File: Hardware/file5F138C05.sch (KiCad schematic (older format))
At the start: 7 parts

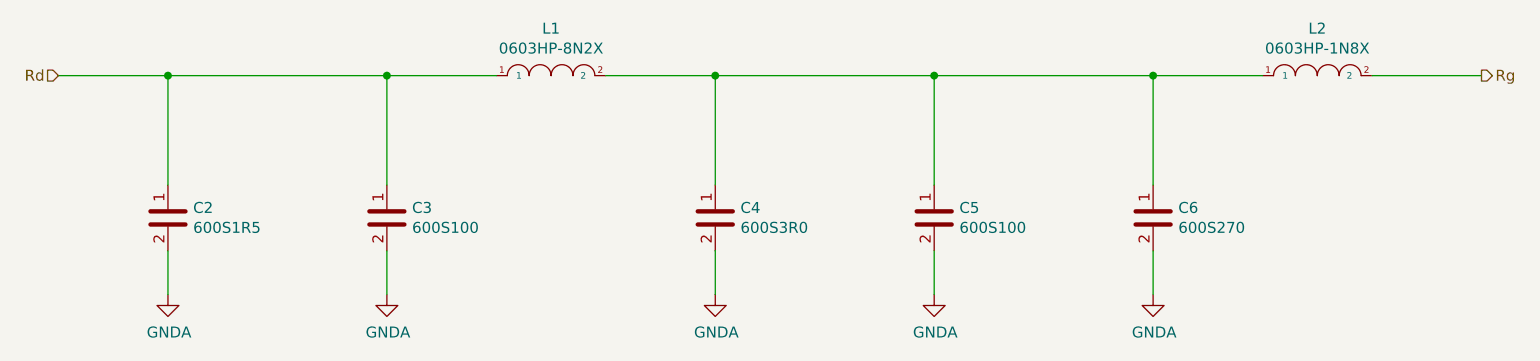
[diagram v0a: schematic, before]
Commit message: Added discrete Chebyshev input filter to schematic based on Qucs simulationd. Artwork not done. It has occurred to me that I need to do some major cleanup of the test points on this PCBA.
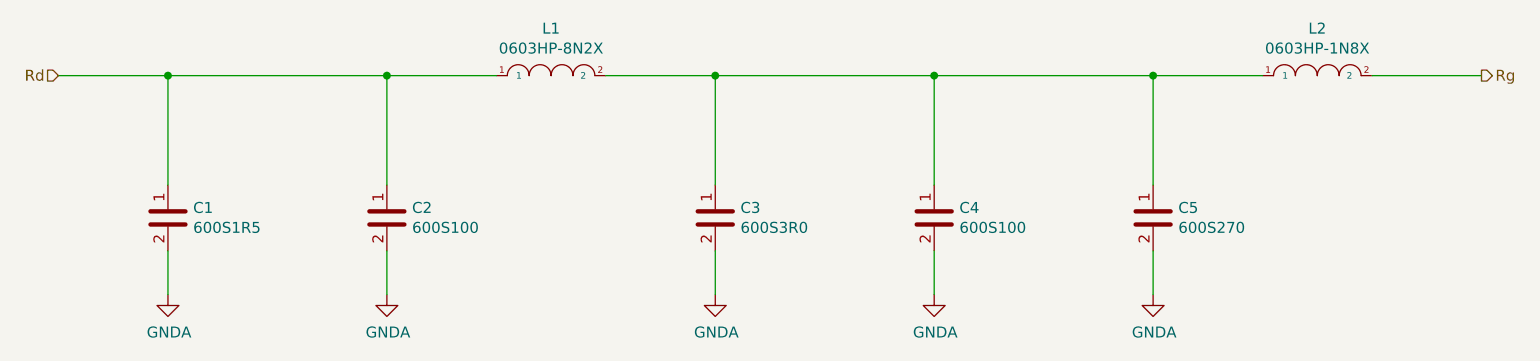
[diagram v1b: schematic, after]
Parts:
- renumbered C2 to C1, C3 to C2, C4 to C3, C5 to C4, C6 to C5
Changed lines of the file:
@@
 $Descr A4 11693 8268
 encoding utf-8
-Sheet 5 12
+Sheet 5 16
 Title ""
 Date ""
@@
 Rg
 $Comp
-L ATC:600S1R5 C2
+L ATC:600S1R5 C1
 U 1 1 5F152659
 P 3000 4150
-F 0 "C2" H 3115 4196 50  0000 L CNN
+F 0 "C1" H 3115 4196 50  0000 L CNN
 F 1 "600S1R5" H 3115 4105 50  0000 L CNN
 F 2 "Capacitor_SMD:C_0603_1608Metric" H 3050 4250 50  0001 C CNN
@@
 $EndComp
 $Comp
-L ATC:600S100 C3
+L ATC:600S100 C2
 U 1 1 5F152A8E
 P 4000 4150
-F 0 "C3" H 4115 4196 50  0000 L CNN
+F 0 "C2" H 4115 4196 50  0000 L CNN
 F 1 "600S100" H 4115 4105 50  0000 L CNN
 F 2 "Capacitor_SMD:C_0603_1608Metric" H 4050 4250 50  0001 C CNN
@@
 $EndComp
 $Comp
-L ATC:600S3R0 C4
+L ATC:600S3R0 C3
 U 1 1 5F152CBF
 P 5500 4150
-F 0 "C4" H 5615 4196 50  0000 L CNN
+F 0 "C3" H 5615 4196 50  0000 L CNN
 F 1 "600S3R0" H 5615 4105 50  0000 L CNN
 F 2 "Capacitor_SMD:C_0603_1608Metric" H 5550 4250 50  0001 C CNN
@@
 $EndComp
 $Comp
-L ATC:600S100 C5
+L ATC:600S100 C4
 U 1 1 5F152F10
 P 6500 4150
-F 0 "C5" H 6615 4196 50  0000 L CNN
+F 0 "C4" H 6615 4196 50  0000 L CNN
 F 1 "600S100" H 6615 4105 50  0000 L CNN
 F 2 "Capacitor_SMD:C_0603_1608Metric" H 6550 4250 50  0001 C CNN
@@
 $EndComp
 $Comp
-L ATC:600S270 C6
+L ATC:600S270 C5
 U 1 1 5F15313B
 P 7500 4150
-F 0 "C6" H 7615 4196 50  0000 L CNN
+F 0 "C5" H 7615 4196 50  0000 L CNN
 F 1 "600S270" H 7615 4105 50  0000 L CNN
 F 2 "Capacitor_SMD:C_0603_1608Metric" H 7550 4250 50  0001 C CNN
@@
 AR Path="/5F19ABE9/5F15450B" Ref="#PWR?"  Part="1"
 AR Path="/5F04F5B6/5F15450B" Ref="#PWR?"  Part="1"
-AR Path="/5F04F5B6/5F138C06/5F15450B" Ref="#PWR09"  Part="1"
-F 0 "#PWR09" H 3000 4250 50  0001 C CNN
+AR Path="/5F04F5B6/5F138C06/5F15450B" Ref="#PWR06"  Part="1"
+F 0 "#PWR06" H 3000 4250 50  0001 C CNN
 F 1 "GNDA" H 3005 4327 50  0000 C CNN
 F 2 "" H 3000 4500 50  0001 C CNN
@@
 AR Path="/5F19ABE9/5F154511" Ref="#PWR?"  Part="1"
 AR Path="/5F04F5B6/5F154511" Ref="#PWR?"  Part="1"
-AR Path="/5F04F5B6/5F138C06/5F154511" Ref="#PWR010"  Part="1"
-F 0 "#PWR010" H 4000 4250 50  0001 C CNN
+AR Path="/5F04F5B6/5F138C06/5F154511" Ref="#PWR07"  Part="1"
+F 0 "#PWR07" H 4000 4250 50  0001 C CNN
 F 1 "GNDA" H 4005 4327 50  0000 C CNN
 F 2 "" H 4000 4500 50  0001 C CNN
@@
 AR Path="/5F19ABE9/5F1549C9" Ref="#PWR?"  Part="1"
 AR Path="/5F04F5B6/5F1549C9" Ref="#PWR?"  Part="1"
-AR Path="/5F04F5B6/5F138C06/5F1549C9" Ref="#PWR011"  Part="1"
-F 0 "#PWR011" H 5500 4250 50  0001 C CNN
+AR Path="/5F04F5B6/5F138C06/5F1549C9" Ref="#PWR08"  Part="1"
+F 0 "#PWR08" H 5500 4250 50  0001 C CNN
 F 1 "GNDA" H 5505 4327 50  0000 C CNN
 F 2 "" H 5500 4500 50  0001 C CNN
@@
 AR Path="/5F19ABE9/5F1549CF" Ref="#PWR?"  Part="1"
 AR Path="/5F04F5B6/5F1549CF" Ref="#PWR?"  Part="1"
-AR Path="/5F04F5B6/5F138C06/5F1549CF" Ref="#PWR012"  Part="1"
-F 0 "#PWR012" H 6500 4250 50  0001 C CNN
+AR Path="/5F04F5B6/5F138C06/5F1549CF" Ref="#PWR09"  Part="1"
+F 0 "#PWR09" H 6500 4250 50  0001 C CNN
 F 1 "GNDA" H 6505 4327 50  0000 C CNN
 F 2 "" H 6500 4500 50  0001 C CNN
@@
 AR Path="/5F19ABE9/5F154DAF" Ref="#PWR?"  Part="1"
 AR Path="/5F04F5B6/5F154DAF" Ref="#PWR?"  Part="1"
-AR Path="/5F04F5B6/5F138C06/5F154DAF" Ref="#PWR013"  Part="1"
-F 0 "#PWR013" H 7500 4250 50  0001 C CNN
+AR Path="/5F04F5B6/5F138C06/5F154DAF" Ref="#PWR010"  Part="1"
+F 0 "#PWR010" H 7500 4250 50  0001 C CNN
 F 1 "GNDA" H 7505 4327 50  0000 C CNN
 F 2 "" H 7500 4500 50  0001 C CNN

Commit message: Major cleanup to both the schematic and directory structure. Stackup has changed accomodate to 0.65mm trace width. Chebyshev filter lived through the experience in the Qucs simulation; others not checked yet. I do want to re-visit the matching networks of all of the amplifiers as I have developed some good strategies to implement them.
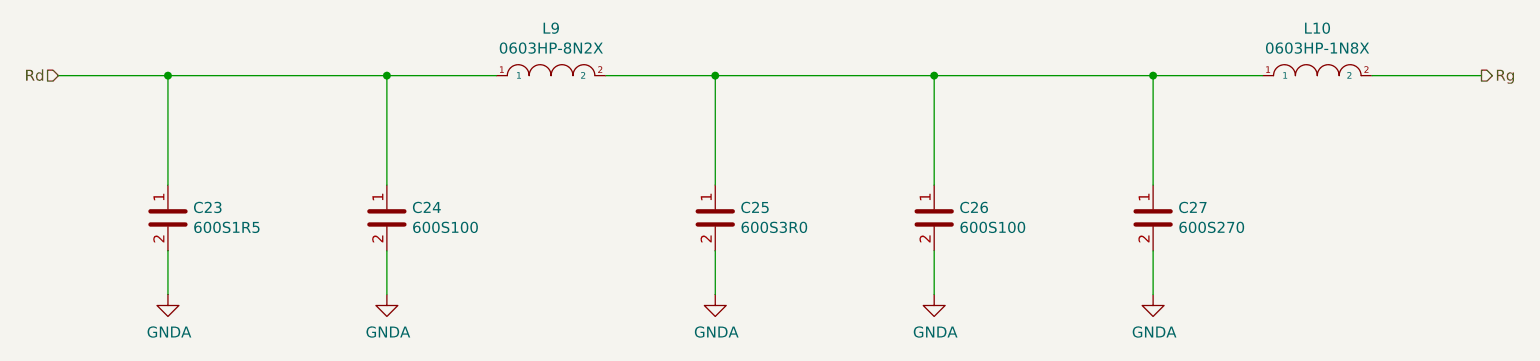
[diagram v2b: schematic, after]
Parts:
- renumbered C1 to C23, C2 to C24, C3 to C25, C4 to C26, C5 to C27, L2 to L10, L1 to L9
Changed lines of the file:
@@
 $Descr A4 11693 8268
 encoding utf-8
-Sheet 5 16
+Sheet 16 24
 Title ""
 Date ""
@@
 Rg
 $Comp
-L ATC:600S1R5 C1
+L ATC:600S1R5 C23
 U 1 1 5F152659
 P 3000 4150
-F 0 "C1" H 3115 4196 50  0000 L CNN
+F 0 "C23" H 3115 4196 50  0000 L CNN
 F 1 "600S1R5" H 3115 4105 50  0000 L CNN
 F 2 "Capacitor_SMD:C_0603_1608Metric" H 3050 4250 50  0001 C CNN
@@
 $EndComp
 $Comp
-L ATC:600S100 C2
+L ATC:600S100 C24
 U 1 1 5F152A8E
 P 4000 4150
-F 0 "C2" H 4115 4196 50  0000 L CNN
+F 0 "C24" H 4115 4196 50  0000 L CNN
 F 1 "600S100" H 4115 4105 50  0000 L CNN
 F 2 "Capacitor_SMD:C_0603_1608Metric" H 4050 4250 50  0001 C CNN
@@
 $EndComp
 $Comp
-L ATC:600S3R0 C3
+L ATC:600S3R0 C25
 U 1 1 5F152CBF
 P 5500 4150
-F 0 "C3" H 5615 4196 50  0000 L CNN
+F 0 "C25" H 5615 4196 50  0000 L CNN
 F 1 "600S3R0" H 5615 4105 50  0000 L CNN
 F 2 "Capacitor_SMD:C_0603_1608Metric" H 5550 4250 50  0001 C CNN
@@
 $EndComp
 $Comp
-L ATC:600S100 C4
+L ATC:600S100 C26
 U 1 1 5F152F10
 P 6500 4150
-F 0 "C4" H 6615 4196 50  0000 L CNN
+F 0 "C26" H 6615 4196 50  0000 L CNN
 F 1 "600S100" H 6615 4105 50  0000 L CNN
 F 2 "Capacitor_SMD:C_0603_1608Metric" H 6550 4250 50  0001 C CNN
@@
 $EndComp
 $Comp
-L ATC:600S270 C5
+L ATC:600S270 C27
 U 1 1 5F15313B
 P 7500 4150
-F 0 "C5" H 7615 4196 50  0000 L CNN
+F 0 "C27" H 7615 4196 50  0000 L CNN
 F 1 "600S270" H 7615 4105 50  0000 L CNN
 F 2 "Capacitor_SMD:C_0603_1608Metric" H 7550 4250 50  0001 C CNN
@@
 $EndComp
 $Comp
-L Coilcraft:0603HP-8N2X L1
+L Coilcraft:0603HP-8N2X L9
 U 1 1 5F1533B1
 P 4750 3500
-F 0 "L1" H 4750 3715 50  0000 C CNN
+F 0 "L9" H 4750 3715 50  0000 C CNN
 F 1 "0603HP-8N2X" H 4750 3624 50  0000 C CNN
 F 2 "Inductor_SMD:L_0603_1608Metric" H 4500 3650 50  0001 C CNN
@@
 $EndComp
 $Comp
-L Coilcraft:0603HP-1N8X L2
+L Coilcraft:0603HP-1N8X L10
 U 1 1 5F1537BD
 P 8250 3500
-F 0 "L2" H 8250 3715 50  0000 C CNN
+F 0 "L10" H 8250 3715 50  0000 C CNN
 F 1 "0603HP-1N8X" H 8250 3624 50  0000 C CNN
 F 2 "Inductor_SMD:L_0603_1608Metric" H 8000 3650 50  0001 C CNN
@@
 AR Path="/5F19ABE9/5F15450B" Ref="#PWR?"  Part="1"
 AR Path="/5F04F5B6/5F15450B" Ref="#PWR?"  Part="1"
-AR Path="/5F04F5B6/5F138C06/5F15450B" Ref="#PWR06"  Part="1"
-F 0 "#PWR06" H 3000 4250 50  0001 C CNN
+AR Path="/5F04F5B6/5F138C06/5F15450B" Ref="#PWR?"  Part="1"
+AR Path="/5F204DEC/5F205D8E/5F138C06/5F15450B" Ref="#PWR029"  Part="1"
+F 0 "#PWR029" H 3000 4250 50  0001 C CNN
 F 1 "GNDA" H 3005 4327 50  0000 C CNN
 F 2 "" H 3000 4500 50  0001 C CNN
@@
 AR Path="/5F19ABE9/5F154511" Ref="#PWR?"  Part="1"
 AR Path="/5F04F5B6/5F154511" Ref="#PWR?"  Part="1"
-AR Path="/5F04F5B6/5F138C06/5F154511" Ref="#PWR07"  Part="1"
-F 0 "#PWR07" H 4000 4250 50  0001 C CNN
+AR Path="/5F04F5B6/5F138C06/5F154511" Ref="#PWR?"  Part="1"
+AR Path="/5F204DEC/5F205D8E/5F138C06/5F154511" Ref="#PWR030"  Part="1"
+F 0 "#PWR030" H 4000 4250 50  0001 C CNN
 F 1 "GNDA" H 4005 4327 50  0000 C CNN
 F 2 "" H 4000 4500 50  0001 C CNN
@@
 AR Path="/5F19ABE9/5F1549C9" Ref="#PWR?"  Part="1"
 AR Path="/5F04F5B6/5F1549C9" Ref="#PWR?"  Part="1"
-AR Path="/5F04F5B6/5F138C06/5F1549C9" Ref="#PWR08"  Part="1"
-F 0 "#PWR08" H 5500 4250 50  0001 C CNN
+AR Path="/5F04F5B6/5F138C06/5F1549C9" Ref="#PWR?"  Part="1"
+AR Path="/5F204DEC/5F205D8E/5F138C06/5F1549C9" Ref="#PWR031"  Part="1"
+F 0 "#PWR031" H 5500 4250 50  0001 C CNN
 F 1 "GNDA" H 5505 4327 50  0000 C CNN
 F 2 "" H 5500 4500 50  0001 C CNN
@@
 AR Path="/5F19ABE9/5F1549CF" Ref="#PWR?"  Part="1"
 AR Path="/5F04F5B6/5F1549CF" Ref="#PWR?"  Part="1"
-AR Path="/5F04F5B6/5F138C06/5F1549CF" Ref="#PWR09"  Part="1"
-F 0 "#PWR09" H 6500 4250 50  0001 C CNN
+AR Path="/5F04F5B6/5F138C06/5F1549CF" Ref="#PWR?"  Part="1"
+AR Path="/5F204DEC/5F205D8E/5F138C06/5F1549CF" Ref="#PWR032"  Part="1"
+F 0 "#PWR032" H 6500 4250 50  0001 C CNN
 F 1 "GNDA" H 6505 4327 50  0000 C CNN
 F 2 "" H 6500 4500 50  0001 C CNN
@@
 AR Path="/5F19ABE9/5F154DAF" Ref="#PWR?"  Part="1"
 AR Path="/5F04F5B6/5F154DAF" Ref="#PWR?"  Part="1"
-AR Path="/5F04F5B6/5F138C06/5F154DAF" Ref="#PWR010"  Part="1"
-F 0 "#PWR010" H 7500 4250 50  0001 C CNN
+AR Path="/5F04F5B6/5F138C06/5F154DAF" Ref="#PWR?"  Part="1"
+AR Path="/5F204DEC/5F205D8E/5F138C06/5F154DAF" Ref="#PWR033"  Part="1"
+F 0 "#PWR033" H 7500 4250 50  0001 C CNN
 F 1 "GNDA" H 7505 4327 50  0000 C CNN
 F 2 "" H 7500 4500 50  0001 C CNN

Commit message: Improving LNA simulations and Documentation package. More to come on this one.
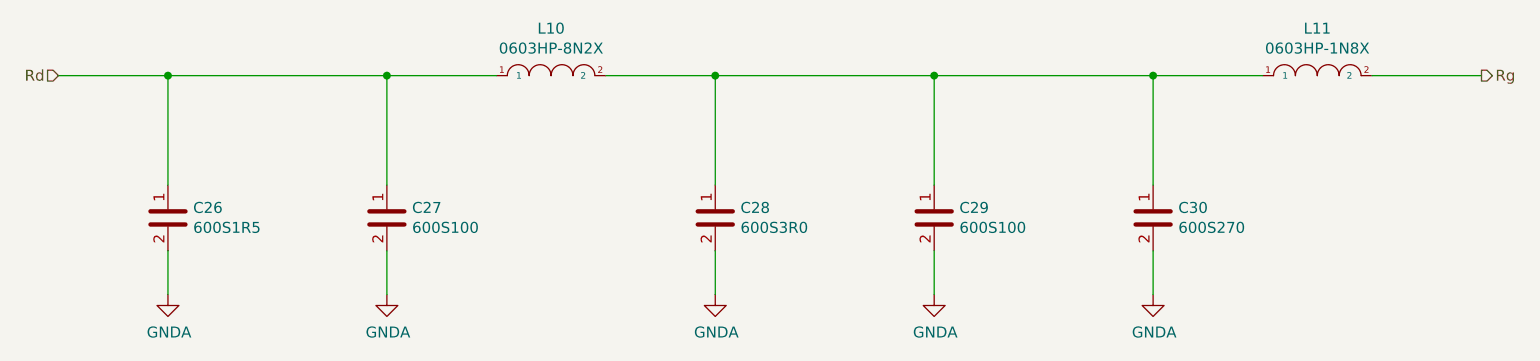
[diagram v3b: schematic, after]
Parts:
- renumbered C23 to C26, C24 to C27, C25 to C28, C26 to C29, C27 to C30, L9 to L10, L10 to L11
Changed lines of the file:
@@
 $Descr A4 11693 8268
 encoding utf-8
-Sheet 16 24
+Sheet 16 23
 Title ""
 Date ""
@@
 Rg
 $Comp
-L ATC:600S1R5 C23
+L ATC:600S1R5 C26
 U 1 1 5F152659
 P 3000 4150
-F 0 "C23" H 3115 4196 50  0000 L CNN
+F 0 "C26" H 3115 4196 50  0000 L CNN
 F 1 "600S1R5" H 3115 4105 50  0000 L CNN
 F 2 "Capacitor_SMD:C_0603_1608Metric" H 3050 4250 50  0001 C CNN
@@
 $EndComp
 $Comp
-L ATC:600S100 C24
+L ATC:600S100 C27
 U 1 1 5F152A8E
 P 4000 4150
-F 0 "C24" H 4115 4196 50  0000 L CNN
+F 0 "C27" H 4115 4196 50  0000 L CNN
 F 1 "600S100" H 4115 4105 50  0000 L CNN
 F 2 "Capacitor_SMD:C_0603_1608Metric" H 4050 4250 50  0001 C CNN
@@
 $EndComp
 $Comp
-L ATC:600S3R0 C25
+L ATC:600S3R0 C28
 U 1 1 5F152CBF
 P 5500 4150
-F 0 "C25" H 5615 4196 50  0000 L CNN
+F 0 "C28" H 5615 4196 50  0000 L CNN
 F 1 "600S3R0" H 5615 4105 50  0000 L CNN
 F 2 "Capacitor_SMD:C_0603_1608Metric" H 5550 4250 50  0001 C CNN
@@
 $EndComp
 $Comp
-L ATC:600S100 C26
+L ATC:600S100 C29
 U 1 1 5F152F10
 P 6500 4150
-F 0 "C26" H 6615 4196 50  0000 L CNN
+F 0 "C29" H 6615 4196 50  0000 L CNN
 F 1 "600S100" H 6615 4105 50  0000 L CNN
 F 2 "Capacitor_SMD:C_0603_1608Metric" H 6550 4250 50  0001 C CNN
@@
 $EndComp
 $Comp
-L ATC:600S270 C27
+L ATC:600S270 C30
 U 1 1 5F15313B
 P 7500 4150
-F 0 "C27" H 7615 4196 50  0000 L CNN
+F 0 "C30" H 7615 4196 50  0000 L CNN
 F 1 "600S270" H 7615 4105 50  0000 L CNN
 F 2 "Capacitor_SMD:C_0603_1608Metric" H 7550 4250 50  0001 C CNN
@@
 $EndComp
 $Comp
-L Coilcraft:0603HP-8N2X L9
+L Coilcraft:0603HP-8N2X L10
 U 1 1 5F1533B1
 P 4750 3500
-F 0 "L9" H 4750 3715 50  0000 C CNN
+F 0 "L10" H 4750 3715 50  0000 C CNN
 F 1 "0603HP-8N2X" H 4750 3624 50  0000 C CNN
 F 2 "Inductor_SMD:L_0603_1608Metric" H 4500 3650 50  0001 C CNN
@@
 $EndComp
 $Comp
-L Coilcraft:0603HP-1N8X L10
+L Coilcraft:0603HP-1N8X L11
 U 1 1 5F1537BD
 P 8250 3500
-F 0 "L10" H 8250 3715 50  0000 C CNN
+F 0 "L11" H 8250 3715 50  0000 C CNN
 F 1 "0603HP-1N8X" H 8250 3624 50  0000 C CNN
 F 2 "Inductor_SMD:L_0603_1608Metric" H 8000 3650 50  0001 C CNN
@@
 AR Path="/5F04F5B6/5F15450B" Ref="#PWR?"  Part="1"
 AR Path="/5F04F5B6/5F138C06/5F15450B" Ref="#PWR?"  Part="1"
-AR Path="/5F204DEC/5F205D8E/5F138C06/5F15450B" Ref="#PWR029"  Part="1"
-F 0 "#PWR029" H 3000 4250 50  0001 C CNN
+AR Path="/5F204DEC/5F205D8E/5F138C06/5F15450B" Ref="#PWR031"  Part="1"
+F 0 "#PWR031" H 3000 4250 50  0001 C CNN
 F 1 "GNDA" H 3005 4327 50  0000 C CNN
 F 2 "" H 3000 4500 50  0001 C CNN
@@
 AR Path="/5F04F5B6/5F154511" Ref="#PWR?"  Part="1"
 AR Path="/5F04F5B6/5F138C06/5F154511" Ref="#PWR?"  Part="1"
-AR Path="/5F204DEC/5F205D8E/5F138C06/5F154511" Ref="#PWR030"  Part="1"
-F 0 "#PWR030" H 4000 4250 50  0001 C CNN
+AR Path="/5F204DEC/5F205D8E/5F138C06/5F154511" Ref="#PWR032"  Part="1"
+F 0 "#PWR032" H 4000 4250 50  0001 C CNN
 F 1 "GNDA" H 4005 4327 50  0000 C CNN
 F 2 "" H 4000 4500 50  0001 C CNN
@@
 AR Path="/5F04F5B6/5F1549C9" Ref="#PWR?"  Part="1"
 AR Path="/5F04F5B6/5F138C06/5F1549C9" Ref="#PWR?"  Part="1"
-AR Path="/5F204DEC/5F205D8E/5F138C06/5F1549C9" Ref="#PWR031"  Part="1"
-F 0 "#PWR031" H 5500 4250 50  0001 C CNN
+AR Path="/5F204DEC/5F205D8E/5F138C06/5F1549C9" Ref="#PWR033"  Part="1"
+F 0 "#PWR033" H 5500 4250 50  0001 C CNN
 F 1 "GNDA" H 5505 4327 50  0000 C CNN
 F 2 "" H 5500 4500 50  0001 C CNN
@@
 AR Path="/5F04F5B6/5F1549CF" Ref="#PWR?"  Part="1"
 AR Path="/5F04F5B6/5F138C06/5F1549CF" Ref="#PWR?"  Part="1"
-AR Path="/5F204DEC/5F205D8E/5F138C06/5F1549CF" Ref="#PWR032"  Part="1"
-F 0 "#PWR032" H 6500 4250 50  0001 C CNN
+AR Path="/5F204DEC/5F205D8E/5F138C06/5F1549CF" Ref="#PWR034"  Part="1"
+F 0 "#PWR034" H 6500 4250 50  0001 C CNN
 F 1 "GNDA" H 6505 4327 50  0000 C CNN
 F 2 "" H 6500 4500 50  0001 C CNN
@@
 AR Path="/5F04F5B6/5F154DAF" Ref="#PWR?"  Part="1"
 AR Path="/5F04F5B6/5F138C06/5F154DAF" Ref="#PWR?"  Part="1"
-AR Path="/5F204DEC/5F205D8E/5F138C06/5F154DAF" Ref="#PWR033"  Part="1"
-F 0 "#PWR033" H 7500 4250 50  0001 C CNN
+AR Path="/5F204DEC/5F205D8E/5F138C06/5F154DAF" Ref="#PWR035"  Part="1"
+F 0 "#PWR035" H 7500 4250 50  0001 C CNN
 F 1 "GNDA" H 7505 4327 50  0000 C CNN
 F 2 "" H 7500 4500 50  0001 C CNN
